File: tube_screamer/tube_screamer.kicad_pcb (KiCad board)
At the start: 2 copper layers, 80 x 100 mm, 67 parts, among them J1 Jack_6.35, J2 Jack_6.35, J6 Barrel_Jack_Switch, J7 Conn_01x01_Socket, J8 Conn_01x01_Socket, J9 top_panel_connector, P1 front_plate, P2 bottom_plate, Q1 MMBT5551, Q10 AO3401A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

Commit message: Updated libraries.
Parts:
- SW1: footprint pedale:foot_switch_tht_and_floating -> pedale:foot_switch_tht_no_pad
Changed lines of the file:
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@@
 		(sheetfile "tube_screamer.kicad_sch")
 		(attr through_hole dnp)
-		(fp_line
-			(start 3.1 8.75)
-			(end -51.4 8.75)
-			(stroke
-				(width 0.12)
-				(type solid)
-			)
-			(layer "F.SilkS")
-		)
-		(fp_line
-			(start 3.1 -21.45)
-			(end 3.1 8.75)
-			(stroke
-				(width 0.12)
-				(type solid)
-			)
-			(layer "F.SilkS")
-		)
-		(fp_line
-			(start -51.4 8.75)
-			(end -51.4 -21.45)
-			(stroke
-				(width 0.12)
-				(type solid)
-			)
-			(layer "F.SilkS")
-		)
-		(fp_line
-			(start -51.4 -21.45)
-			(end 3.1 -21.45)
-			(stroke
-				(width 0.12)
-				(type solid)
-			)
-			(layer "F.SilkS")
-		)
-		(fp_line
-			(start 3.6 9.25)
-			(end -51.9 9.25)
-			(stroke
-				(width 0.05)
-				(type solid)
-			)
-			(layer "F.CrtYd")
-		)
-		(fp_line
-			(start 3.6 -21.95)
-			(end 3.6 9.25)
-			(stroke
-				(width 0.05)
-				(type solid)
-			)
-			(layer "F.CrtYd")
-		)
-		(fp_line
-			(start -51.9 9.25)
-			(end -51.9 -21.95)
-			(stroke
-				(width 0.05)
-				(type solid)
-			)
-			(layer "F.CrtYd")
-		)
-		(fp_line
-			(start -51.9 -21.95)
-			(end 3.6 -21.95)
+		(fp_rect
+			(start -51.4 -21.4)
+			(end 3.1 8.8)
 			(stroke
 				(width 0.05)
-				(type solid)
+				(type default)
 			)
+			(fill no)
 			(layer "F.CrtYd")
 		)
@@
 		)
 	)
-	(footprint "pedale:foot_switch_tht_and_floating"
+	(footprint "pedale:foot_switch_tht_no_pad"
 		(locked yes)
 		(layer "F.Cu")
@@
 		(attr through_hole dnp)
 		(fp_rect
-			(start -14.2 -13.2)
-			(end 14.2 13.2)
+			(start -9.2 -7.7)
+			(end 9.2 7.7)
 			(stroke
 				(width 0.05)
@@
 			(layer "F.CrtYd")
 		)
+		(fp_rect
+			(start -9 -7.5)
+			(end 9 7.5)
+			(stroke
+				(width 0.15)
+				(type default)
+			)
+			(fill no)
+			(layer "F.Fab")
+		)
 		(fp_text user "${REFERENCE}"
 			(at -0.1 -10.875 0)
@@
 		)
 		(pad "1" thru_hole roundrect
-			(at -7.1 -5 180)
-			(size 8.8 11.6)
-			(drill oval 2 4
-				(offset 2.4 2.2)
-			)
+			(at -7.1 -4.5 180)
+			(size 4 5)
+			(drill oval 2 3)
 			(layers "*.Cu" "*.Mask")
 			(remove_unused_layers no)
-			(roundrect_rratio 0.1136363636)
+			(roundrect_rratio 0.25)
 			(net 25 "/SW_ON")
 			(pinfunction "A")
@@
 		)
 		(pad "2" thru_hole roundrect
-			(at 0 -5)
-			(size 4 11.5)
-			(drill oval 2 4
-				(offset 0 -2.25)
-			)
+			(at 0 -4.5)
+			(size 4 5)
+			(drill oval 2 3)
 			(layers "*.Cu" "*.Mask")
 			(remove_unused_layers no)
@@
 		)
 		(pad "3" thru_hole roundrect
-			(at 7.1 -5 180)
-			(size 8.9 11.5)
-			(drill oval 2 4
-				(offset -2.45 2.25)
-			)
+			(at 7.1 -4.5 180)
+			(size 4 5)
+			(drill oval 2 3)
 			(layers "*.Cu" "*.Mask")
 			(remove_unused_layers no)
-			(roundrect_rratio 0.1123595506)
+			(roundrect_rratio 0.25)
 			(net 15 "IN_BUFF")
 			(pinfunction "C")
@@
 		)
 		(pad "4" thru_hole roundrect
-			(at 7.1 5)
-			(size 8.9 11.5)
-			(drill oval 2 4
-				(offset 2.45 2.25)
-			)
+			(at 7.1 4.5)
+			(size 4 5)
+			(drill oval 2 3)
 			(layers "*.Cu" "*.Mask")
 			(remove_unused_layers no)
-			(roundrect_rratio 0.1123595506)
+			(roundrect_rratio 0.25)
 			(net 12 "9V")
 			(pinfunction "A")
@@
 		)
 		(pad "5" thru_hole roundrect
-			(at 0 5)
-			(size 4 11.5)
-			(drill oval 2 4
-				(offset 0 2.25)
-			)
+			(at 0 4.5)
+			(size 4 5)
+			(drill oval 2 3)
 			(layers "*.Cu" "*.Mask")
 			(remove_unused_layers no)
@@
 		)
 		(pad "6" thru_hole roundrect
-			(at -7.1 5)
-			(size 8.9 11.5)
-			(drill oval 2 4
-				(offset -2.45 2.25)
-			)
+			(at -7.1 4.5)
+			(size 4 5)
+			(drill oval 2 3)
 			(layers "*.Cu" "*.Mask")
 			(remove_unused_layers no)
-			(roundrect_rratio 0.1123595506)
+			(roundrect_rratio 0.25)
 			(net 44 "unconnected-(SW1B-C-Pad6)")
 			(pinfunction "C")
@@
 		(sheetfile "tube_screamer.kicad_sch")
 		(attr through_hole dnp)
-		(fp_line
-			(start 26.4 18.23)
-			(end 26.4 -2)
-			(stroke
-				(width 0.05)
-				(type solid)
-			)
-			(layer "F.CrtYd")
-		)
-		(fp_line
-			(start 26.4 -2)
-			(end -7.45 -2)
-			(stroke
-				(width 0.05)
-				(type solid)
-			)
-			(layer "F.CrtYd")
-		)
-		(fp_line
-			(start -7.45 18.23)
-			(end 26.4 18.23)
-			(stroke
-				(width 0.05)
-				(type solid)
-			)
-			(layer "F.CrtYd")
-		)
-		(fp_line
-			(start -7.45 18.23)
-			(end -7.45 -2)
+		(fp_rect
+			(start -7 -1)
+			(end 26.4 17.3)
 			(stroke
 				(width 0.05)
-				(type solid)
+				(type default)
 			)
+			(fill no)
 			(layer "F.CrtYd")
 		)
@@
 		(sheetfile "tube_screamer.kicad_sch")
 		(attr through_hole dnp)
-		(fp_line
-			(start -7.45 18.23)
-			(end -7.45 -2)
-			(stroke
-				(width 0.05)
-				(type solid)
-			)
-			(layer "F.CrtYd")
-		)
-		(fp_line
-			(start -7.45 18.23)
-			(end 26.4 18.23)
-			(stroke
-				(width 0.05)
-				(type solid)
-			)
-			(layer "F.CrtYd")
-		)
-		(fp_line
-			(start 26.4 -2)
-			(end -7.45 -2)
-			(stroke
-				(width 0.05)
-				(type solid)
-			)
-			(layer "F.CrtYd")
-		)
-		(fp_line
-			(start 26.4 18.23)
-			(end 26.4 -2)
+		(fp_rect
+			(start -7 -1)
+			(end 26.4 17.3)
 			(stroke
 				(width 0.05)
-				(type solid)
+				(type default)
 			)
+			(fill no)
 			(layer "F.CrtYd")
 		)
@@
 			)
 			(fill no)
-			(layer "B.CrtYd")
+			(layer "F.CrtYd")
 		)
 		(fp_text user "${REFERENCE}"

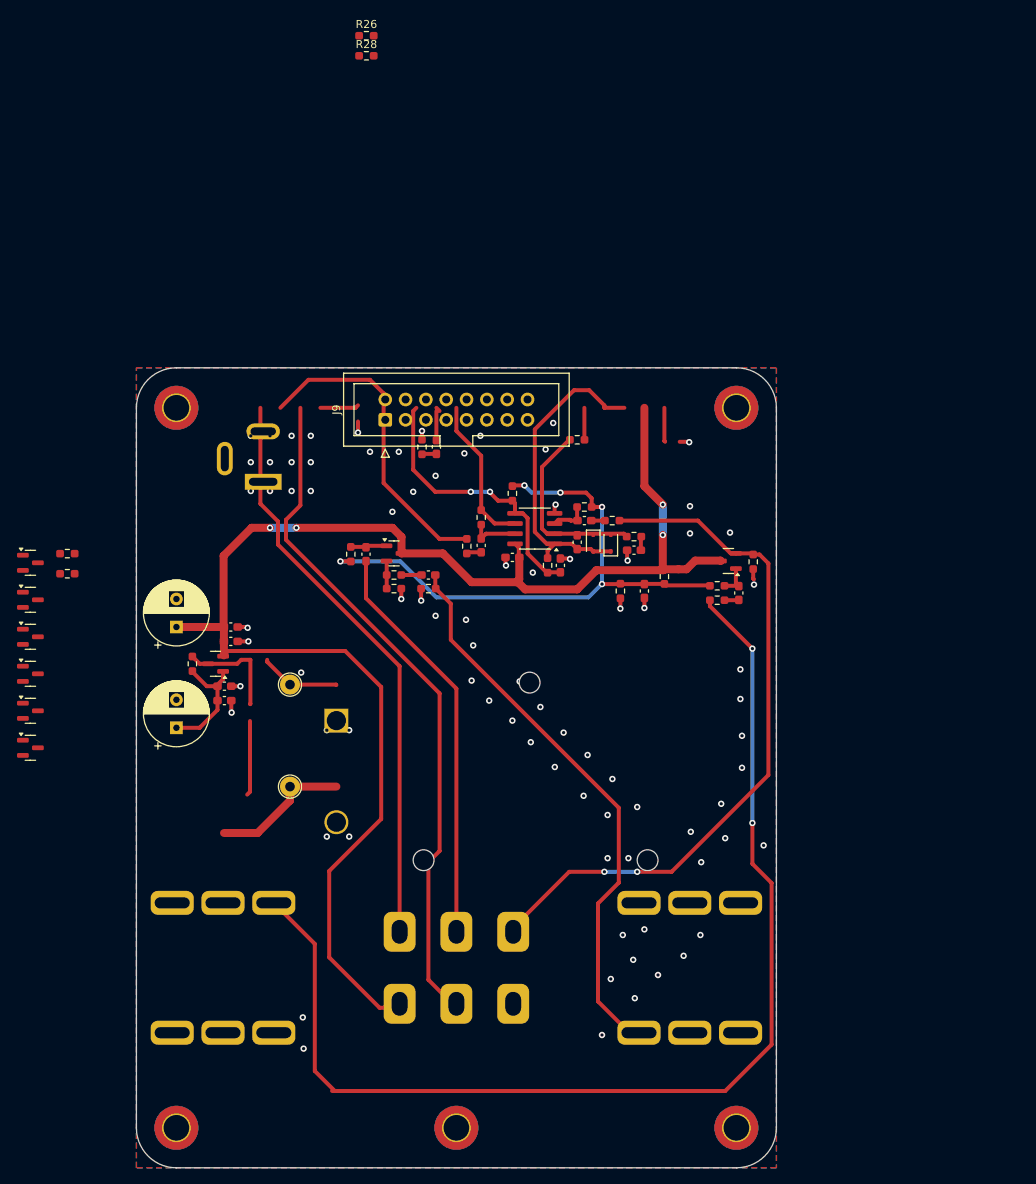
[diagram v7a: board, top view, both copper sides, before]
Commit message: IDC connector moved.
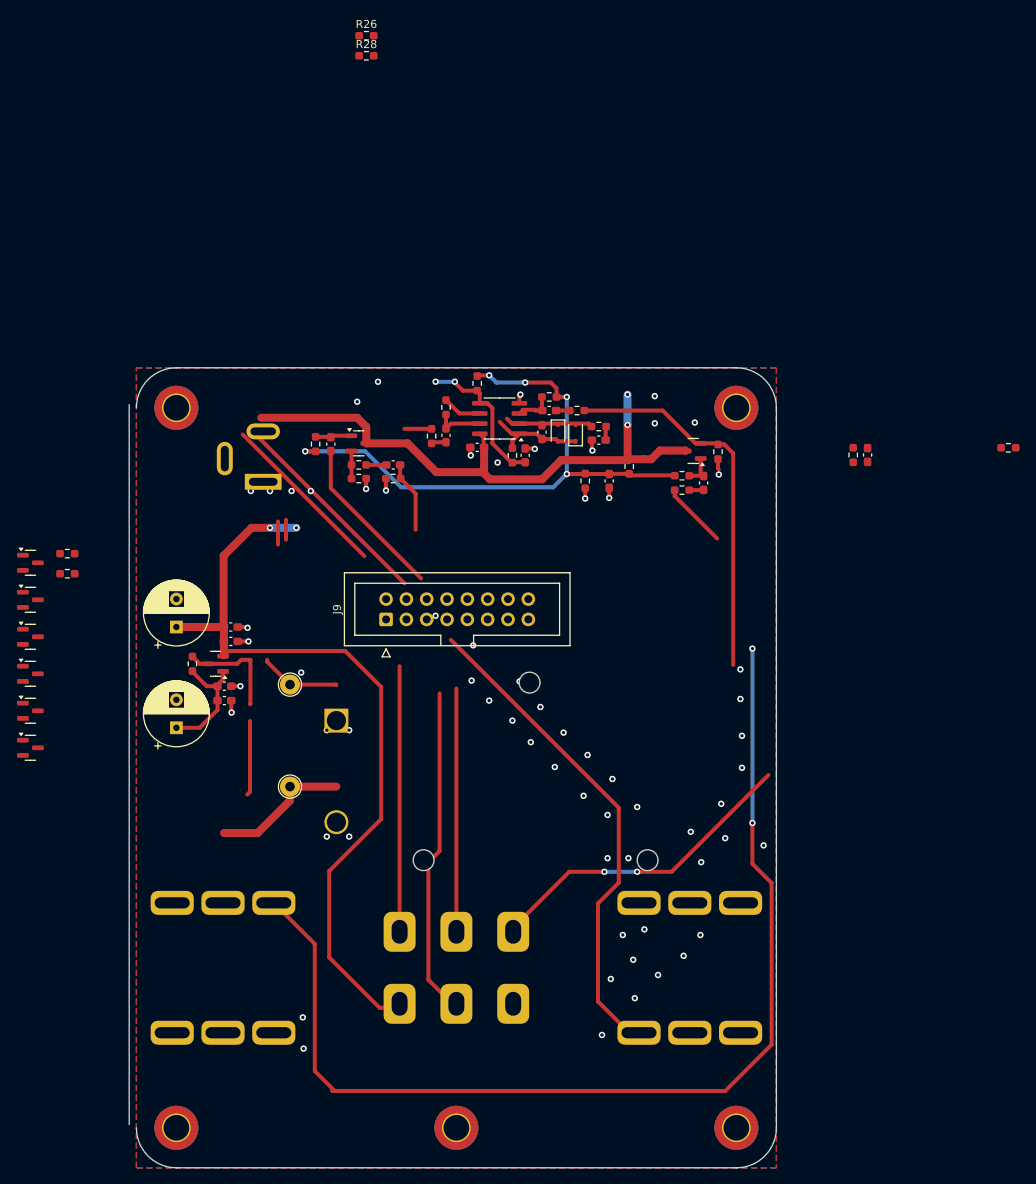
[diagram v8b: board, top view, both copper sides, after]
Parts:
- moved C6 53.9 mm to (141.4, 60.9)
- moved R47 53.9 mm to (159.0, 60.0)
- moved R7 53.9 mm to (139.6, 60.9)
- moved J9 25.0 mm to (81.2, 81.5)
- moved C11 14.4 mm to (82.1, 62.1)
- moved Q1 14.4 mm to (119.6, 60.4)
- moved R11 14.4 mm to (77.8, 62.1)
- moved R3 14.4 mm to (101.6, 53.6)
- moved C1 14.4 mm to (107.8, 59.0)
- moved C12 14.4 mm to (74.3, 59.5)
- moved C14 14.4 mm to (109.1, 64.1)
- moved C17 14.4 mm to (92.6, 59.9)
- moved C4 14.4 mm to (98.6, 60.9)
- moved D1 14.4 mm to (102.7, 58.1)
- moved D2 14.4 mm to (104.9, 58.1)
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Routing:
- net unconnected-(J2-PadTN): track 0.00 -> 134.5 mm, vias 0 -> 2
- net unconnected-(J1-PadTN): track 142.8 -> 61.7 mm, vias 2 -> 0
- net /OUTPUT: track 70.6 -> 8.90 mm
- net /SW_ON: track 72.2 -> 35.6 mm
- net OP_OUT: track 39.5 -> 3.41 mm
- net /OVD: track 39.8 -> 12.7 mm
- net CONN+: track 9.34 -> 30.8 mm
- net /TON_LOW: track 35.1 -> 18.9 mm
- net /RED_LED: track 85.7 -> 71.0 mm
- net /TON_HIGH: track 19.0 -> 4.92 mm
- net 9V: track 184.2 -> 171.2 mm
- net Net-(D1-K): track 23.5 -> 10.9 mm
- net (no net): track 9.12 -> 0.00 mm
- net /INPUT: track 0.00 -> 8.34 mm
- net Net-(J9B-Pin_7): track 4.20 -> 0.00 mm
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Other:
- board size 80 x 100 mm -> 80.9 x 100 mm
